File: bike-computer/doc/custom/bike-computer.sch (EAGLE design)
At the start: 3 parts

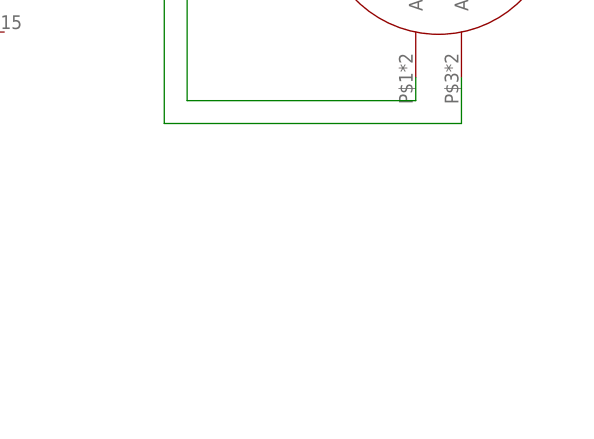
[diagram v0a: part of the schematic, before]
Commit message: [Bike] Add a simple 0.9 inch OLED device. It fits to the hausing.
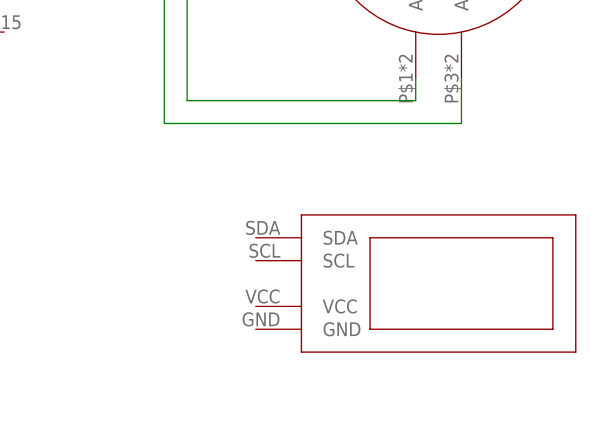
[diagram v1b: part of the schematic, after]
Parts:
- added U$3: OLED_0.9, bike_computer:OLED_0.9
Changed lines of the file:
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@@
 <part name="SUPPLY21" library="supply2" library_urn="urn:adsk.eagle:library:372" deviceset="0V" device=""/>
 <part name="SUPPLY22" library="supply2" library_urn="urn:adsk.eagle:library:372" deviceset="0V" device=""/>
+<part name="U$3" library="bike_computer" deviceset="OLED_0.9" device=""/>
 </parts>
 <sheets>
@@
 <attribute name="VALUE" x="24.257" y="-42.672" size="1.778" layer="96"/>
 </instance>
+<instance part="U$3" gate="OLED_0.9" x="137.16" y="-38.1" smashed="yes"/>
 </instances>
 <busses>

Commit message: [Bike] Some changes for bike-computer
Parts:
- renumbered U$2 to DRV8825
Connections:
- new net SCL: ARDUINO_NANO1.A5, U$3.SCL
- new net SDA: ARDUINO_NANO1.A4, U$3.SDA
- net +5V: now also U$3.VCC
- net 0V: now also U$3.GND
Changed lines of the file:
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@@
 <part name="U$1" library="bike_computer" deviceset="STEPPER_GAUGE" device=""/>
 <part name="ARDUINO_NANO1" library="ArduinoNanoV30" deviceset="ARDUINO_NANO" device=""/>
-<part name="U$2" library="bike_computer" deviceset="DRV8825_BOARD" device=""/>
 <part name="SUPPLY1" library="supply2" library_urn="urn:adsk.eagle:library:372" deviceset="+5V" device=""/>
 <part name="SUPPLY2" library="supply2" library_urn="urn:adsk.eagle:library:372" deviceset="+5V" device=""/>
@@
 <part name="SUPPLY22" library="supply2" library_urn="urn:adsk.eagle:library:372" deviceset="0V" device=""/>
 <part name="U$3" library="bike_computer" deviceset="OLED_0.9" device=""/>
+<part name="DRV8825" library="bike_computer" deviceset="DRV8825_BOARD" device=""/>
 </parts>
 <sheets>
@@
 <attribute name="VALUE" x="-27.94" y="-20.32" size="1.778" layer="96"/>
 </instance>
-<instance part="U$2" gate="G$1" x="71.12" y="2.54" smashed="yes"/>
 <instance part="SUPPLY1" gate="+5V" x="-22.86" y="-35.56" smashed="yes">
 <attribute name="VALUE" x="-24.765" y="-32.385" size="1.778" layer="96"/>
@@
 <attribute name="VALUE" x="-14.605" y="-34.925" size="1.778" layer="96"/>
 </instance>
-<instance part="SUPPLY3" gate="+5V" x="-2.54" y="-38.1" smashed="yes">
-<attribute name="VALUE" x="-4.445" y="-34.925" size="1.778" layer="96"/>
+<instance part="SUPPLY3" gate="+5V" x="91.44" y="-40.64" smashed="yes">
+<attribute name="VALUE" x="89.535" y="-37.465" size="1.778" layer="96"/>
 </instance>
 <instance part="SUPPLY4" gate="+5V" x="43.18" y="2.54" smashed="yes">
@@
 <attribute name="VALUE" x="29.337" y="-37.592" size="1.778" layer="96"/>
 </instance>
-<instance part="SUPPLY22" gate="0V" x="25.4" y="-40.64" smashed="yes">
-<attribute name="VALUE" x="24.257" y="-42.672" size="1.778" layer="96"/>
-</instance>
-<instance part="U$3" gate="OLED_0.9" x="137.16" y="-38.1" smashed="yes"/>
+<instance part="SUPPLY22" gate="0V" x="91.44" y="-50.8" smashed="yes">
+<attribute name="VALUE" x="90.297" y="-52.832" size="1.778" layer="96"/>
+</instance>
+<instance part="U$3" gate="OLED_0.9" x="134.62" y="-40.64" smashed="yes"/>
+<instance part="DRV8825" gate="G$1" x="71.12" y="2.54" smashed="yes">
+<attribute name="NAME" x="63.5" y="-15.24" size="1.778" layer="95"/>
+</instance>
 </instances>
 <busses>
@@
 <net name="N$1" class="0">
 <segment>
-<pinref part="U$2" gate="G$1" pin="B2"/>
 <pinref part="U$1" gate="G$1" pin="B2"/>
 <wire x1="86.36" y1="5.08" x2="116.84" y2="5.08" width="0.1524" layer="91"/>
+<pinref part="DRV8825" gate="G$1" pin="B2"/>
 </segment>
 </net>
 <net name="N$2" class="0">
 <segment>
-<pinref part="U$2" gate="G$1" pin="B1"/>
 <wire x1="86.36" y1="2.54" x2="109.22" y2="2.54" width="0.1524" layer="91"/>
 <wire x1="109.22" y1="2.54" x2="109.22" y2="0" width="0.1524" layer="91"/>
 <pinref part="U$1" gate="G$1" pin="B1"/>
 <wire x1="109.22" y1="0" x2="116.84" y2="0" width="0.1524" layer="91"/>
+<pinref part="DRV8825" gate="G$1" pin="B1"/>
 </segment>
 </net>
 <net name="N$3" class="0">
 <segment>
-<pinref part="U$2" gate="G$1" pin="A2"/>
 <wire x1="86.36" y1="0" x2="106.68" y2="0" width="0.1524" layer="91"/>
 <wire x1="106.68" y1="0" x2="106.68" y2="-17.78" width="0.1524" layer="91"/>
@@
 <wire x1="106.68" y1="-17.78" x2="132.08" y2="-17.78" width="0.1524" layer="91"/>
 <wire x1="132.08" y1="-17.78" x2="132.08" y2="-15.24" width="0.1524" layer="91"/>
+<pinref part="DRV8825" gate="G$1" pin="A2"/>
 </segment>
 </net>
 <net name="N$4" class="0">
 <segment>
-<pinref part="U$2" gate="G$1" pin="A1"/>
 <wire x1="86.36" y1="-2.54" x2="104.14" y2="-2.54" width="0.1524" layer="91"/>
 <wire x1="104.14" y1="-2.54" x2="104.14" y2="-20.32" width="0.1524" layer="91"/>
@@
 <wire x1="104.14" y1="-20.32" x2="137.16" y2="-20.32" width="0.1524" layer="91"/>
 <wire x1="137.16" y1="-20.32" x2="137.16" y2="-15.24" width="0.1524" layer="91"/>
+<pinref part="DRV8825" gate="G$1" pin="A1"/>
 </segment>
 </net>
@@
 <segment>
 <pinref part="SUPPLY19" gate="0V" pin="0V"/>
-<pinref part="U$2" gate="G$1" pin="GNDLOGIC"/>
 <wire x1="93.98" y1="12.7" x2="88.9" y2="12.7" width="0.1524" layer="91"/>
-<pinref part="U$2" gate="G$1" pin="GNDMOT"/>
 <wire x1="88.9" y1="12.7" x2="86.36" y2="12.7" width="0.1524" layer="91"/>
 <wire x1="86.36" y1="15.24" x2="88.9" y2="15.24" width="0.1524" layer="91"/>
 <wire x1="88.9" y1="15.24" x2="88.9" y2="12.7" width="0.1524" layer="91"/>
 <junction x="88.9" y="12.7"/>
+<pinref part="DRV8825" gate="G$1" pin="GNDMOT"/>
+<pinref part="DRV8825" gate="G$1" pin="GNDLOGIC"/>
 </segment>
 <segment>
 <pinref part="SUPPLY18" gate="0V" pin="0V"/>
-<pinref part="U$2" gate="G$1" pin="ENABLE"/>
 <wire x1="48.26" y1="7.62" x2="55.88" y2="7.62" width="0.1524" layer="91"/>
+<pinref part="DRV8825" gate="G$1" pin="ENABLE"/>
 </segment>
 <segment>
@@
 <wire x1="12.7" y1="35.56" x2="12.7" y2="33.02" width="0.1524" layer="91"/>
 </segment>
+<segment>
+<pinref part="U$3" gate="OLED_0.9" pin="GND"/>
+<pinref part="SUPPLY22" gate="0V" pin="0V"/>
+<wire x1="111.76" y1="-45.72" x2="91.44" y2="-45.72" width="0.1524" layer="91"/>
+<wire x1="91.44" y1="-45.72" x2="91.44" y2="-48.26" width="0.1524" layer="91"/>
+</segment>
 </net>
 <net name="+12V" class="0">
 <segment>
-<pinref part="U$2" gate="G$1" pin="VMOT"/>
 <pinref part="SUPPLY9" gate="+12V" pin="+12V"/>
 <wire x1="86.36" y1="17.78" x2="91.44" y2="17.78" width="0.1524" layer="91"/>
 <wire x1="91.44" y1="17.78" x2="91.44" y2="22.86" width="0.1524" layer="91"/>
+<pinref part="DRV8825" gate="G$1" pin="VMOT"/>
 </segment>
 </net>
@@
 <pinref part="SUPPLY4" gate="+5V" pin="+5V"/>
 <wire x1="43.18" y1="0" x2="43.18" y2="-5.08" width="0.1524" layer="91"/>
-<pinref part="U$2" gate="G$1" pin="SLEEP"/>
 <wire x1="43.18" y1="-5.08" x2="53.34" y2="-5.08" width="0.1524" layer="91"/>
-<pinref part="U$2" gate="G$1" pin="RESET"/>
 <wire x1="53.34" y1="-5.08" x2="55.88" y2="-5.08" width="0.1524" layer="91"/>
 <wire x1="55.88" y1="-2.54" x2="53.34" y2="-2.54" width="0.1524" layer="91"/>
 <wire x1="53.34" y1="-2.54" x2="53.34" y2="-5.08" width="0.1524" layer="91"/>
 <junction x="53.34" y="-5.08"/>
+<pinref part="DRV8825" gate="G$1" pin="RESET"/>
+<pinref part="DRV8825" gate="G$1" pin="SLEEP"/>
 </segment>
 <segment>
@@
 <wire x1="17.78" y1="17.78" x2="17.78" y2="20.32" width="0.1524" layer="91"/>
 </segment>
+<segment>
+<pinref part="U$3" gate="OLED_0.9" pin="VCC"/>
+<pinref part="SUPPLY3" gate="+5V" pin="+5V"/>
+<wire x1="111.76" y1="-43.18" x2="91.44" y2="-43.18" width="0.1524" layer="91"/>
+</segment>
 </net>
 <net name="STEP" class="0">
 <segment>
-<pinref part="U$2" gate="G$1" pin="STEP"/>
 <wire x1="55.88" y1="-7.62" x2="43.18" y2="-7.62" width="0.1524" layer="91"/>
 <label x="35.56" y="-7.62" size="1.778" layer="95"/>
+<pinref part="DRV8825" gate="G$1" pin="STEP"/>
 </segment>
 <segment>
@@
 <net name="DIR" class="0">
 <segment>
-<pinref part="U$2" gate="G$1" pin="DIR"/>
 <wire x1="55.88" y1="-10.16" x2="43.18" y2="-10.16" width="0.1524" layer="91"/>
 <label x="35.56" y="-10.16" size="1.778" layer="95"/>
+<pinref part="DRV8825" gate="G$1" pin="DIR"/>
 </segment>
 <segment>
@@
 </segment>
 </net>
+<net name="SDA" class="0">
+<segment>
+<pinref part="U$3" gate="OLED_0.9" pin="SDA"/>
+<wire x1="111.76" y1="-35.56" x2="106.68" y2="-35.56" width="0.1524" layer="91"/>
+<label x="99.06" y="-35.56" size="1.778" layer="95"/>
+</segment>
+<segment>
+<pinref part="ARDUINO_NANO1" gate="G$1" pin="A4"/>
+<wire x1="7.62" y1="7.62" x2="12.7" y2="7.62" width="0.1524" layer="91"/>
+<label x="15.24" y="7.62" size="1.778" layer="95"/>
+</segment>
+</net>
+<net name="SCL" class="0">
+<segment>
+<pinref part="U$3" gate="OLED_0.9" pin="SCL"/>
+<wire x1="111.76" y1="-38.1" x2="106.68" y2="-38.1" width="0.1524" layer="91"/>
+<label x="99.06" y="-38.1" size="1.778" layer="95"/>
+</segment>
+<segment>
+<pinref part="ARDUINO_NANO1" gate="G$1" pin="A5"/>
+<wire x1="7.62" y1="10.16" x2="12.7" y2="10.16" width="0.1524" layer="91"/>
+<label x="15.24" y="10.16" size="1.778" layer="95"/>
+</segment>
+</net>

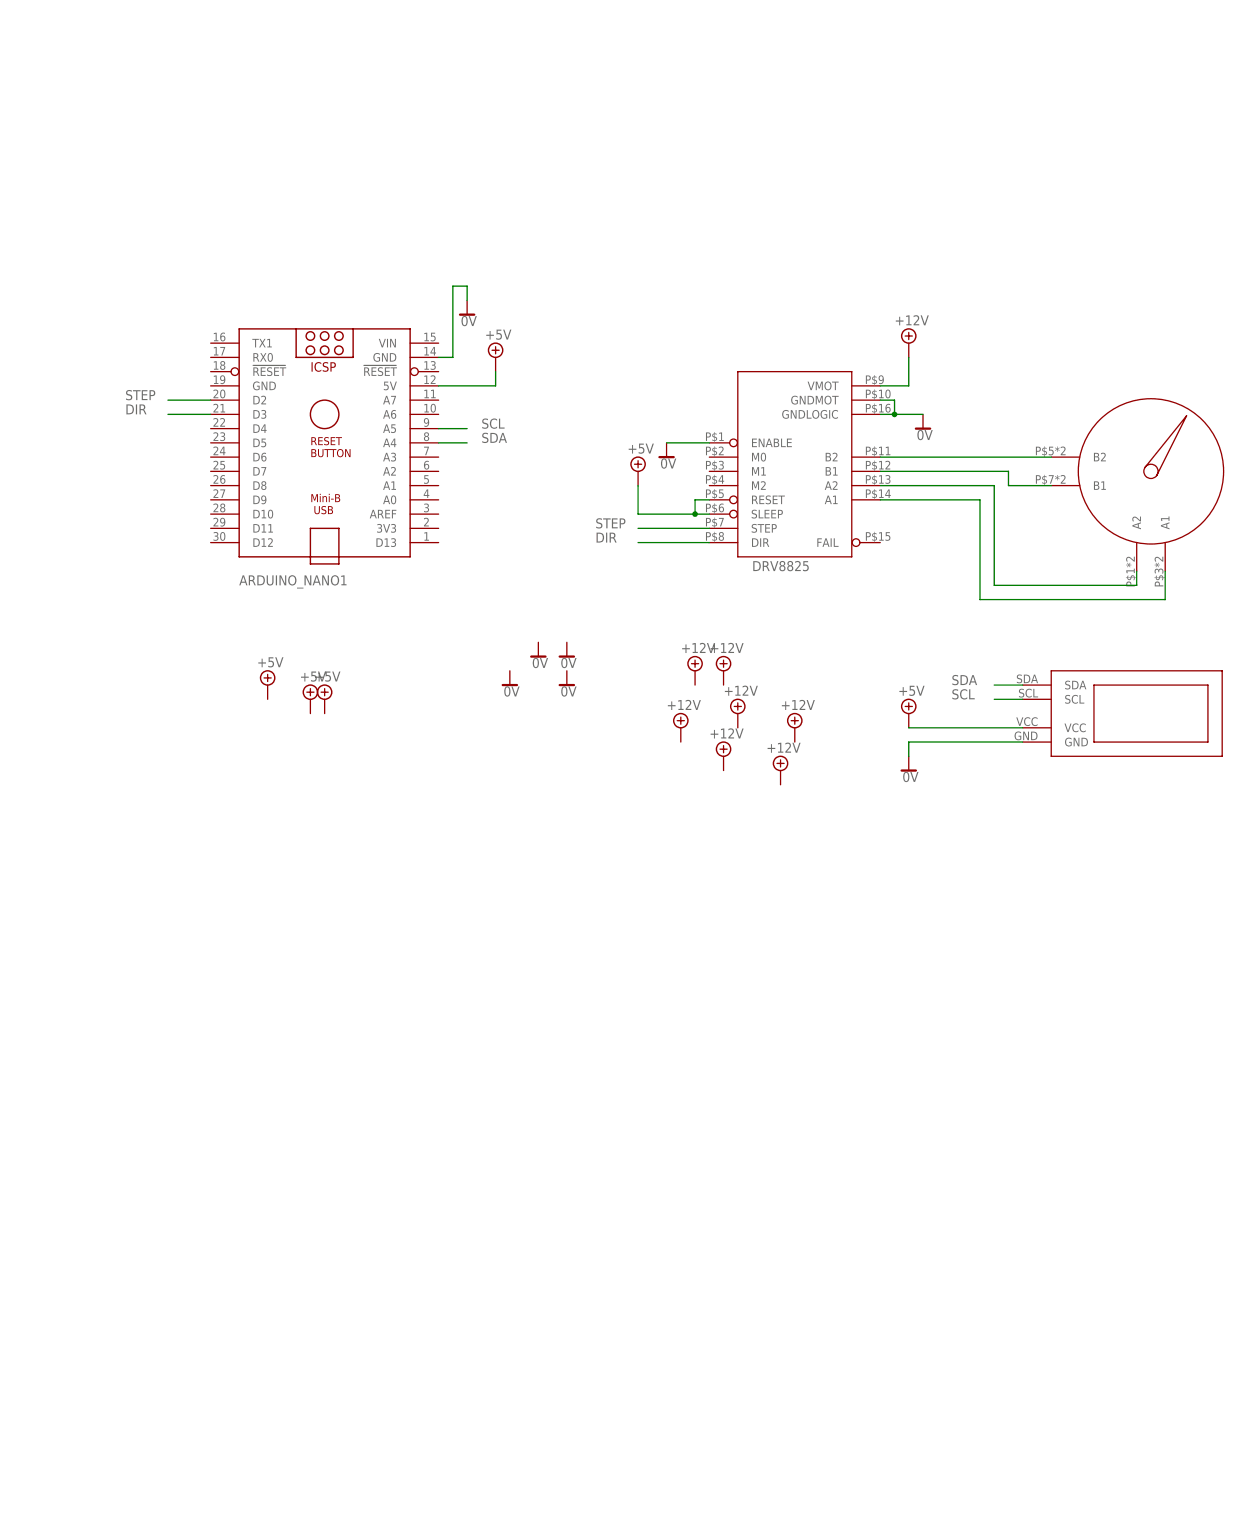
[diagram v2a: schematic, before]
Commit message: [Bike] Further work on schematics.
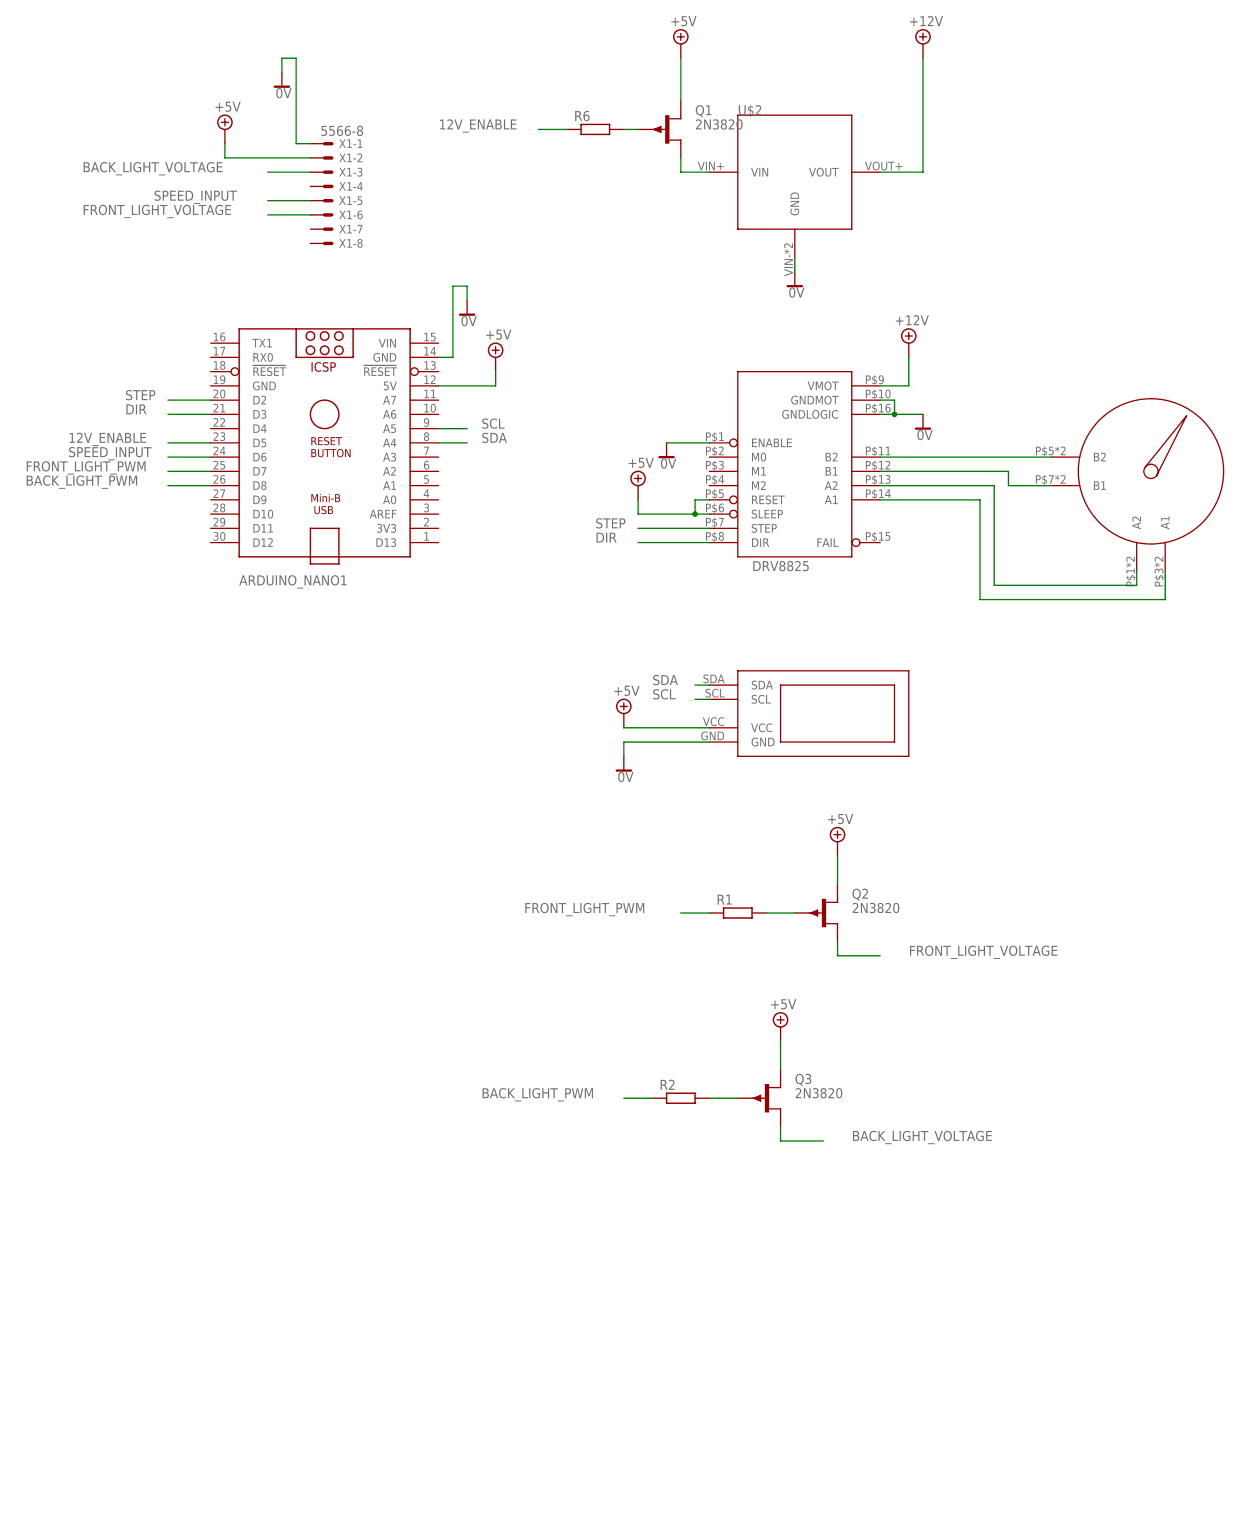
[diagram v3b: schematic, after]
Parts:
- added Q1, Q2, Q3: 2N3820, transistor-small-signal:2N3820
- added R1, R2, R6: (no value), rcl:R-EU_0204/5
- added U$2: STEP_UP_REG, bike_computer:STEP_UP_REG
- added X1: 5566-8, con-molex:5566-8
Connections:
- new net 12V_ENABLE: ARDUINO_NANO1.D5, R6.1
- new net BACK_LIGHT_PWM: ARDUINO_NANO1.D8, R2.1
- new net BACK_LIGHT_VOLTAGE: Q3.D, X1-3.S
- new net FRONT_LIGHT_PWM: ARDUINO_NANO1.D7, R1.1
- new net FRONT_LIGHT_VOLTAGE: Q2.D, X1-6.S
- new net N$5: Q2.G, R1.2
- new net N$6: Q1.G, R6.2
- new net N$7: Q1.D, U$2.VIN
- new net N$8: Q3.G, R2.2
- new net SPEED_INPUT: ARDUINO_NANO1.D6, X1-5.S
- net +12V: now also U$2.VOUT
- net +5V: now also Q1.S, Q2.S, Q3.S, X1-2.S
- net 0V: now also U$2.GND, X1-1.S
